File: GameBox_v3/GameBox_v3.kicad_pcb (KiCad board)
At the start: 2 copper layers, 35.5 x 75.5 mm, 22 parts, among them J1 OLED, J2 Conn_01x08, SW1 ON/OFF, SW2 SW_up, SW3 SW_down, SW4 SW_right, SW5 SW_left, SW6 SW_select, U1 ATmega328P-A, U2 3.3V_boost_regulator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

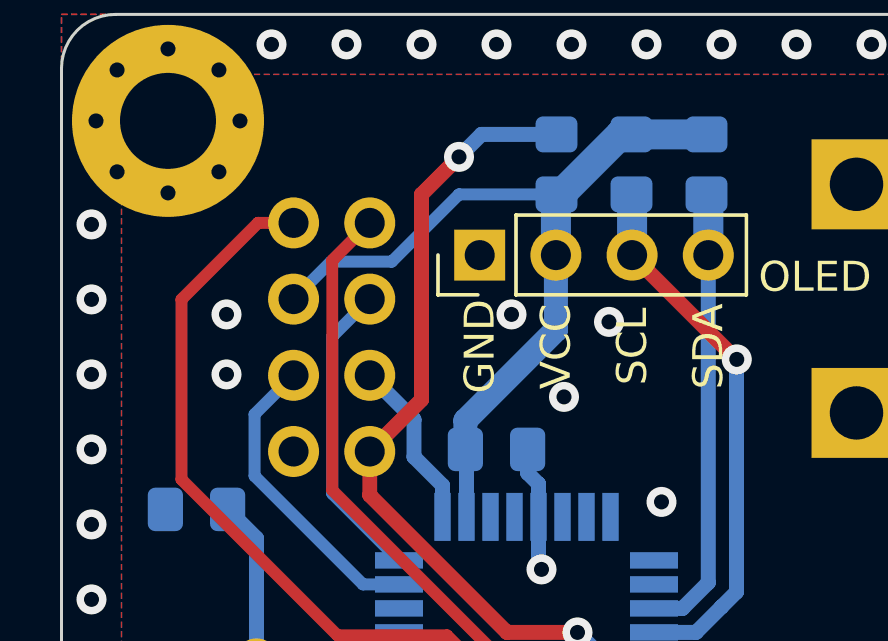
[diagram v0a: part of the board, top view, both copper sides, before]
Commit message: fixed OLEDs
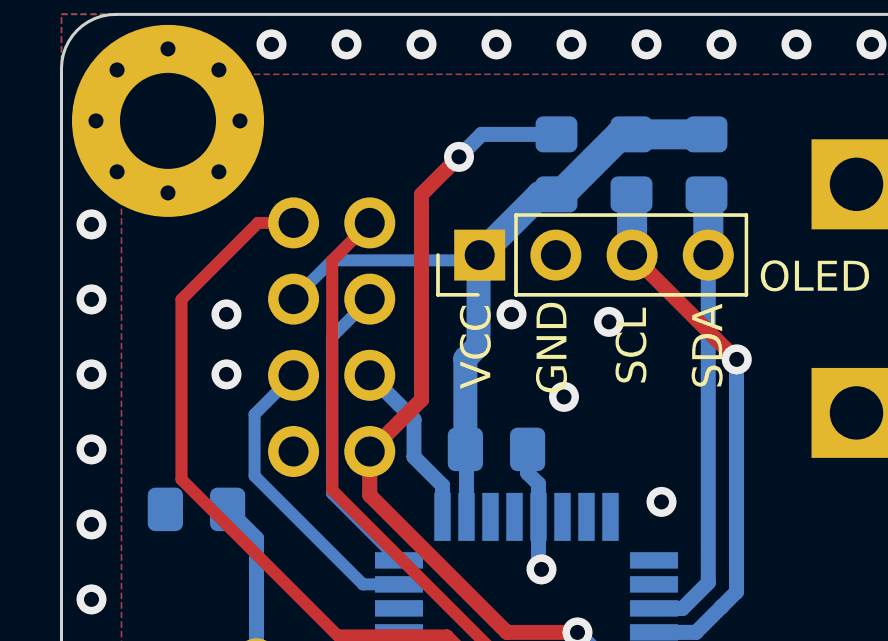
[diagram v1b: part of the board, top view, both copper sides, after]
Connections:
- J1 pad 1: GND -> VCC
- J1 pad 2: VCC -> GND
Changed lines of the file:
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@@
       (effects (font (size 1 1) (thickness 0.15)))
     )
-    (fp_text user "VCC" (at -1.27 -11.684 90 unlocked) (layer "F.SilkS")
+    (fp_text user "VCC" (at -3.92 -11.684 90 unlocked) (layer "F.SilkS")
       (effects (font (size 1 1) (thickness 0.15)))
     )
@@
       (effects (font (size 1 1) (thickness 0.15)))
     )
-    (fp_text user "GND" (at -3.81 -11.684 90 unlocked) (layer "F.SilkS")
+    (fp_text user "GND" (at -1.38 -11.644 90 unlocked) (layer "F.SilkS")
       (effects (font (size 1 1) (thickness 0.15)))
     )
@@
     (fp_line (start -16.764 -16.22) (end 16.764 -16.22) (layer "F.CrtYd") (width 0.05))
     (pad "1" thru_hole rect (at -3.81 -14.726 90) (size 1.7 1.7) (drill 1) (layers *.Cu *.Mask)
-      (net 7 "GND") (pinfunction "Pin_1") (pintype "passive"))
+      (net 1 "VCC") (pinfunction "Pin_1") (pintype "passive"))
     (pad "2" thru_hole oval (at -1.27 -14.726 90) (size 1.7 1.7) (drill 1) (layers *.Cu *.Mask)
-      (net 1 "VCC") (pinfunction "Pin_2") (pintype "passive"))
+      (net 7 "GND") (pinfunction "Pin_2") (pintype "passive"))
     (pad "3" thru_hole oval (at 1.27 -14.726 90) (size 1.7 1.7) (drill 1) (layers *.Cu *.Mask)
       (net 3 "SCL") (pinfunction "Pin_3") (pintype "passive"))
@@
   )
   (segment (start 166.48 81.02) (end 166.5 81) (width 1) (layer "B.Cu") (net 1))
+  (segment (start 159.025489 83.199511) (end 163.764489 83.199511) (width 0.4) (layer "B.Cu") (net 1))
   (segment (start 169 79) (end 168.5 79) (width 0.5) (layer "B.Cu") (net 1))
-  (segment (start 163.4625 88.5375) (end 166.48 85.52) (width 0.8) (layer "B.Cu") (net 1))
-  (segment (start 166.48 85.52) (end 166.48 83.024) (width 0.8) (layer "B.Cu") (net 1))
-  (segment (start 166.48 83.024) (end 166.48 81.02) (width 1) (layer "B.Cu") (net 1))
   (segment (start 164.3 100.25) (end 164.3 103.0125) (width 0.5) (layer "B.Cu") (net 1))
-  (segment (start 161.009511 83.240489) (end 163.25 81) (width 0.4) (layer "B.Cu") (net 1))
-  (segment (start 163.4625 89.5) (end 163.4625 88.5375) (width 0.8) (layer "B.Cu") (net 1))
+  (segment (start 163.900489 83.063511) (end 163.94 83.024) (width 0.8) (layer "B.Cu") (net 1))
+  (segment (start 163.94 83.024) (end 165.964 81) (width 0.9) (layer "B.Cu") (net 1))
+  (segment (start 163.4625 89.5) (end 163.4625 86.4735) (width 0.8) (layer "B.Cu") (net 1))
   (segment (start 166.642824 81) (end 168.642824 79) (width 1) (layer "B.Cu") (net 1))
   (segment (start 163.5 91.75) (end 163.5 89.5375) (width 0.5) (layer "B.Cu") (net 1))
-  (segment (start 163.25 81) (end 166.5 81) (width 0.4) (layer "B.Cu") (net 1))
+  (segment (start 163.764489 83.199511) (end 165.964 81) (width 0.4) (layer "B.Cu") (net 1))
   (segment (start 165.9 101.4) (end 166.5 102) (width 0.5) (layer "B.Cu") (net 1))
+  (segment (start 165.964 81) (end 166.5 81) (width 0.9) (layer "B.Cu") (net 1))
   (segment (start 168.642824 79) (end 169 79) (width 1) (layer "B.Cu") (net 1))
   (segment (start 165.9 100.25) (end 165.9 101.4) (width 0.5) (layer "B.Cu") (net 1))
@@
   (segment (start 164.3 103.0125) (end 164.5 103.2125) (width 0.5) (layer "B.Cu") (net 1))
   (segment (start 163.2875 103.2125) (end 159.23 107.27) (width 1) (layer "B.Cu") (net 1))
-  (segment (start 158.984511 83.240489) (end 161.009511 83.240489) (width 0.4) (layer "B.Cu") (net 1))
+  (segment (start 163.900489 86.035511) (end 163.900489 83.063511) (width 0.8) (layer "B.Cu") (net 1))
+  (segment (start 163.4625 86.4735) (end 163.900489 86.035511) (width 0.8) (layer "B.Cu") (net 1))
+  (segment (start 157.735 84.49) (end 159.025489 83.199511) (width 0.4) (layer "B.Cu") (net 1))
   (segment (start 159.23 107.27) (end 159.23 107.65) (width 1) (layer "B.Cu") (net 1))
   (segment (start 171.5 79) (end 169 79) (width 1) (layer "B.Cu") (net 1))
-  (segment (start 157.735 84.49) (end 158.984511 83.240489) (width 0.4) (layer "B.Cu") (net 1))
   (segment (start 168.5 79) (end 166.5 81) (width 0.5) (layer "B.Cu") (net 1))
   (segment (start 170.7 94.8) (end 169.75 94.8) (width 0.5) (layer "B.Cu") (net 2))
